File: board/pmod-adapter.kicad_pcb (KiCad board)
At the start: 2 copper layers, 20.3 x 86.4 mm, 28 parts

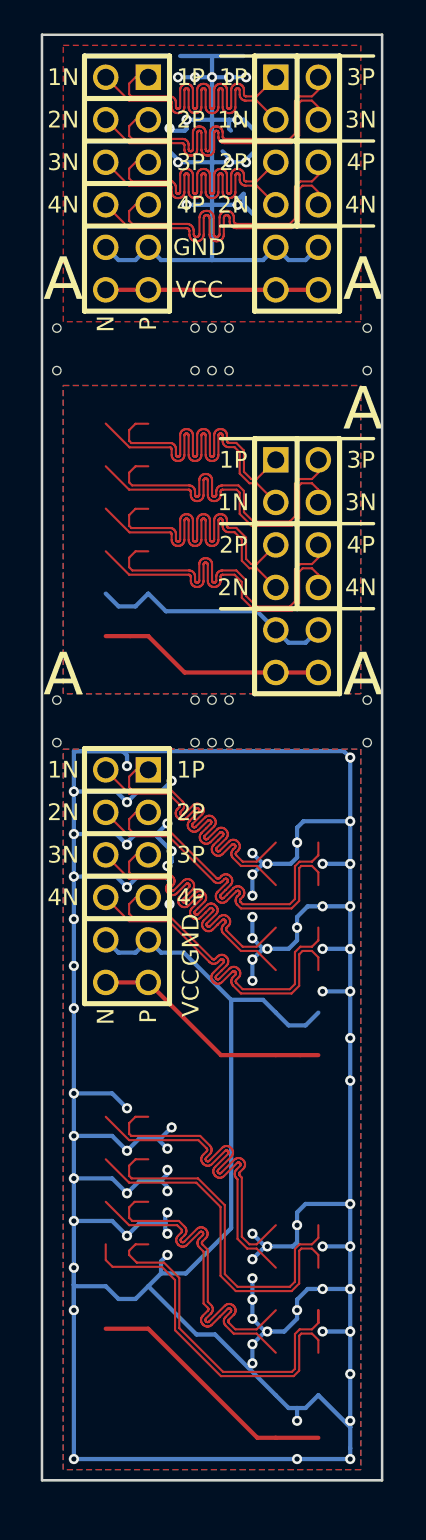
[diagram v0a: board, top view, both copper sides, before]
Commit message: Adding more gnd vias
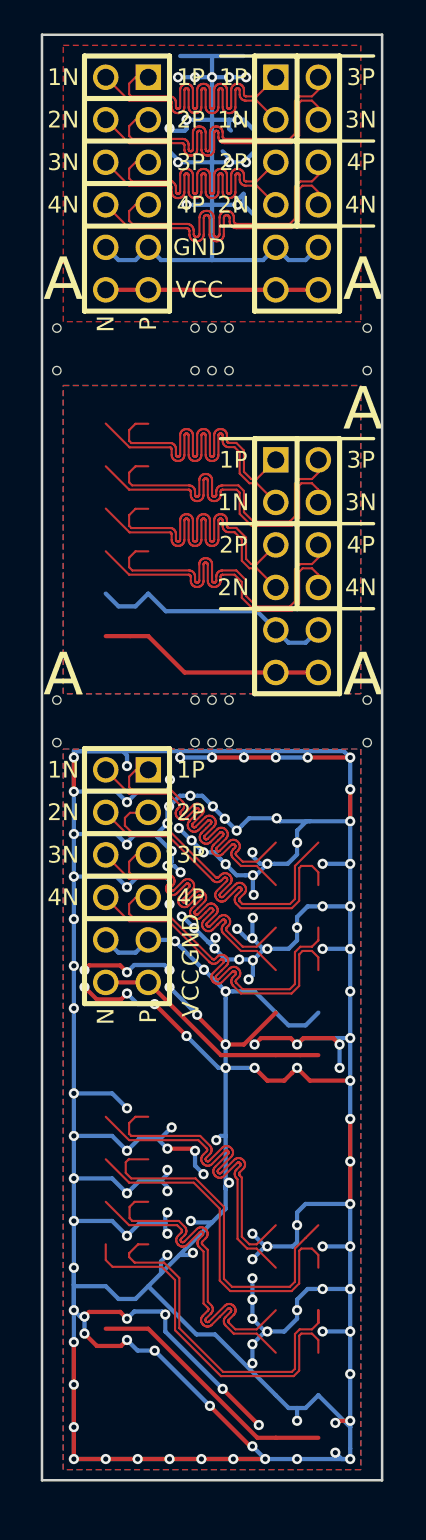
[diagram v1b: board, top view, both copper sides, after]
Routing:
- net /GND34: track 273.8 -> 429.2 mm, vias 73 -> 151
- net (no net): track 10.4 -> 0.00 mm, vias 6 -> 0

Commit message: Temp commit.
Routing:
- net /GND34: track 429.2 -> 452.3 mm, vias 151 -> 166
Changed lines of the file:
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@@
     (thickness 1.6)
     (drawings 28)
-    (tracks 3609)
+    (tracks 3656)
     (zones 0)
     (modules 32)
@@
   (segment (start 48.386999 76.326999) (end 49.53 77.47) (width 0.127) (layer F.Cu) (net 26))
   (segment (start 39.37 70.612) (end 40.767 72.009) (width 0.127) (layer F.Cu) (net 26))
+  (segment (start 37.5666 92.5576) (end 39.37 92.5576) (width 0.254) (layer B.Cu) (net 27))
+  (segment (start 39.37 92.5576) (end 39.8526 92.5576) (width 0.254) (layer B.Cu) (net 27))
+  (via (at 39.37 92.5576) (size 0.6096) (drill 0.3048) (layers F.Cu B.Cu) (net 27))
+  (segment (start 37.5412 89.9922) (end 39.37 89.9922) (width 0.254) (layer B.Cu) (net 27))
+  (segment (start 39.37 89.9922) (end 39.8272 89.9922) (width 0.254) (layer B.Cu) (net 27))
+  (via (at 39.37 89.9922) (size 0.6096) (drill 0.3048) (layers F.Cu B.Cu) (net 27))
+  (segment (start 37.5666 87.4776) (end 39.37 87.4776) (width 0.254) (layer B.Cu) (net 27))
+  (segment (start 39.37 87.4776) (end 39.8526 87.4776) (width 0.254) (layer B.Cu) (net 27))
+  (via (at 39.37 87.4776) (size 0.6096) (drill 0.3048) (layers F.Cu B.Cu) (net 27))
+  (segment (start 37.465 84.836) (end 37.5666 84.9376) (width 0.254) (layer B.Cu) (net 27))
+  (segment (start 37.5666 84.9376) (end 39.8526 84.9376) (width 0.254) (layer B.Cu) (net 27))
+  (segment (start 39.8526 84.9376) (end 40.64 85.725) (width 0.254) (layer B.Cu) (net 27))
+  (segment (start 37.465 92.456) (end 37.5666 92.5576) (width 0.254) (layer B.Cu) (net 27))
+  (segment (start 39.8526 92.5576) (end 40.64 93.345) (width 0.254) (layer B.Cu) (net 27))
+  (segment (start 37.465 89.916) (end 37.5412 89.9922) (width 0.254) (layer B.Cu) (net 27))
+  (segment (start 39.8272 89.9922) (end 40.64 90.805) (width 0.254) (layer B.Cu) (net 27))
+  (segment (start 37.465 87.376) (end 37.5666 87.4776) (width 0.254) (layer B.Cu) (net 27))
+  (segment (start 39.8526 87.4776) (end 40.64 88.265) (width 0.254) (layer B.Cu) (net 27))
+  (segment (start 52.07 102.87) (end 51.1556 101.9556) (width 0.254) (layer F.Cu) (net 27))
+  (via (at 51.1556 101.9556) (size 0.6096) (drill 0.3048) (layers F.Cu B.Cu) (net 27))
+  (segment (start 46.355 102.489) (end 47.8536 102.489) (width 0.254) (layer F.Cu) (net 27))
+  (segment (start 47.8536 102.489) (end 48.0314 102.3112) (width 0.254) (layer F.Cu) (net 27))
+  (via (at 48.0314 102.3112) (size 0.6096) (drill 0.3048) (layers F.Cu B.Cu) (net 27))
+  (segment (start 44.577 94.361) (end 44.577 95.1992) (width 0.254) (layer F.Cu) (net 27))
+  (segment (start 44.577 95.1992) (end 44.2468 95.5294) (width 0.254) (layer F.Cu) (net 27))
+  (via (at 44.2468 95.5294) (size 0.6096) (drill 0.3048) (layers F.Cu B.Cu) (net 27))
+  (segment (start 46.6344 100.8888) (end 44.3484 98.6028) (width 0.254) (layer B.Cu) (net 27))
+  (via (at 44.3484 98.6028) (size 0.6096) (drill 0.3048) (layers F.Cu B.Cu) (net 27))
+  (segment (start 48.133 100.965) (end 46.7106 100.965) (width 0.254) (layer F.Cu) (net 27))
+  (segment (start 46.7106 100.965) (end 46.6344 100.8888) (width 0.254) (layer F.Cu) (net 27))
+  (via (at 46.6344 100.8888) (size 0.6096) (drill 0.3048) (layers F.Cu B.Cu) (net 27))
+  (segment (start 53.975 78.74) (end 53.34 78.74) (width 0.254) (layer F.Cu) (net 27))
+  (segment (start 53.34 78.74) (end 52.07 80.01) (width 0.254) (layer F.Cu) (net 27))
+  (segment (start 43.8404 71.628) (end 44.577 71.628) (width 0.254) (layer B.Cu) (net 27))
+  (segment (start 44.577 71.628) (end 45.1612 72.2122) (width 0.254) (layer B.Cu) (net 27))
+  (via (at 45.1612 72.2122) (size 0.6096) (drill 0.3048) (layers F.Cu B.Cu) (net 27))
+  (segment (start 48.133 93.218) (end 48.133 89.7636) (width 0.254) (layer F.Cu) (net 27))
+  (segment (start 48.133 89.7636) (end 48.0314 89.662) (width 0.254) (layer F.Cu) (net 27))
+  (via (at 48.0314 89.662) (size 0.6096) (drill 0.3048) (layers F.Cu B.Cu) (net 27))
+  (segment (start 46.9392 95.6818) (end 46.9392 94.0562) (width 0.254) (layer B.Cu) (net 27))
+  (segment (start 46.9392 94.0562) (end 46.9646 94.0308) (width 0.254) (layer B.Cu) (net 27))
+  (via (at 46.9646 94.0308) (size 0.6096) (drill 0.3048) (layers F.Cu B.Cu) (net 27))
+  (segment (start 48.133 95.885) (end 47.1424 95.885) (width 0.254) (layer B.Cu) (net 27))
+  (segment (start 47.1424 95.885) (end 46.9392 95.6818) (width 0.254) (layer B.Cu) (net 27))
+  (via (at 46.9392 95.6818) (size 0.6096) (drill 0.3048) (layers F.Cu B.Cu) (net 27))
+  (segment (start 44.0817 98.5266) (end 41.91 96.3549) (width 0.254) (layer B.Cu) (net 27))
+  (segment (start 44.7929 99.2378) (end 44.0817 98.5266) (width 0.254) (layer B.Cu) (net 27))
+  (segment (start 44.0817 98.5266) (end 44.0817 98.4631) (width 0.254) (layer B.Cu) (net 27))
+  (segment (start 44.0817 98.4631) (end 44.8056 97.7392) (width 0.254) (layer B.Cu) (net 27))
+  (via (at 44.8056 97.7392) (size 0.6096) (drill 0.3048) (layers F.Cu B.Cu) (net 27))
+  (segment (start 45.8978 99.2378) (end 45.9232 99.2378) (width 0.254) (layer B.Cu) (net 27))
+  (via (at 46.101 99.06) (size 0.6096) (drill 0.3048) (layers F.Cu B.Cu) (net 27))
+  (segment (start 45.9232 99.2378) (end 46.101 99.06) (width 0.254) (layer B.Cu) (net 27))
+  (segment (start 48.133 97.155) (end 46.101 97.155) (width 0.254) (layer B.Cu) (net 27))
+  (segment (start 46.101 97.155) (end 46.0756 97.1296) (width 0.254) (layer B.Cu) (net 27))
+  (via (at 46.0756 97.1296) (size 0.6096) (drill 0.3048) (layers F.Cu B.Cu) (net 27))
   (via (at 45.212 89.662) (size 0.6096) (drill 0.3048) (layers F.Cu B.Cu) (net 27))
   (segment (start 44.704 88.265) (end 44.704 89.154) (width 0.254) (layer B.Cu) (net 27))
@@
   (segment (start 53.975 76.2) (end 52.324 76.2) (width 0.254) (layer B.Cu) (net 27))
   (via (at 52.324 76.2) (size 0.6096) (drill 0.3048) (layers F.Cu B.Cu) (net 27))
-  (segment (start 37.465 92.456) (end 39.751 92.456) (width 0.254) (layer B.Cu) (net 27))
-  (segment (start 39.751 92.456) (end 40.64 93.345) (width 0.254) (layer B.Cu) (net 27))
   (via (at 40.64 93.345) (size 0.6096) (drill 0.3048) (layers F.Cu B.Cu) (net 27))
-  (segment (start 37.465 84.836) (end 39.751 84.836) (width 0.254) (layer B.Cu) (net 27))
   (via (at 40.64 85.725) (size 0.6096) (drill 0.3048) (layers F.Cu B.Cu) (net 27))
-  (segment (start 39.751 84.836) (end 40.64 85.725) (width 0.254) (layer B.Cu) (net 27))
-  (segment (start 37.465 87.376) (end 39.751 87.376) (width 0.254) (layer B.Cu) (net 27))
-  (segment (start 39.751 87.376) (end 40.64 88.265) (width 0.254) (layer B.Cu) (net 27))
   (via (at 40.64 88.265) (size 0.6096) (drill 0.3048) (layers F.Cu B.Cu) (net 27))
-  (segment (start 37.465 89.916) (end 39.751 89.916) (width 0.254) (layer B.Cu) (net 27))
   (via (at 40.64 90.805) (size 0.6096) (drill 0.3048) (layers F.Cu B.Cu) (net 27))
-  (segment (start 39.751 89.916) (end 40.64 90.805) (width 0.254) (layer B.Cu) (net 27))
   (segment (start 51.308001 103.631999) (end 50.8 103.631999) (width 0.254) (layer B.Cu) (net 27))
   (segment (start 50.8 103.631999) (end 50.291999 103.631999) (width 0.254) (layer B.Cu) (net 27))
@@
   (segment (start 40.131999 97.116899) (end 39.37 96.3549) (width 0.254) (layer B.Cu) (net 27))
   (segment (start 45.8978 99.2378) (end 44.7929 99.2378) (width 0.254) (layer B.Cu) (net 27))
-  (segment (start 44.7929 99.2378) (end 41.91 96.3549) (width 0.254) (layer B.Cu) (net 27))
   (segment (start 49.53 102.87) (end 45.8978 99.2378) (width 0.254) (layer B.Cu) (net 27))
   (segment (start 52.07 102.87) (end 51.308001 103.631999) (width 0.254) (layer B.Cu) (net 27))

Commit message: Slowly adding more vias.
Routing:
- net /GND34: track 452.3 -> 457.4 mm, vias 166 -> 169
- net /J4D_N: track 21.5 -> 20.9 mm
- added copper zone on B.Cu, net /GND1
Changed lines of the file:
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@@
     (thickness 1.6)
     (drawings 28)
-    (tracks 3656)
+    (tracks 3666)
     (zones 0)
     (modules 32)
@@
   (segment (start 48.386999 76.326999) (end 49.53 77.47) (width 0.127) (layer F.Cu) (net 26))
   (segment (start 39.37 70.612) (end 40.767 72.009) (width 0.127) (layer F.Cu) (net 26))
+  (segment (start 48.5648 88.4428) (end 48.2346 88.1126) (width 0.254) (layer F.Cu) (net 27))
+  (segment (start 48.2346 88.1126) (end 47.5488 88.1126) (width 0.254) (layer F.Cu) (net 27))
+  (via (at 47.5488 88.1126) (size 0.6096) (drill 0.3048) (layers F.Cu B.Cu) (net 27))
+  (segment (start 48.5648 89.1286) (end 48.5648 88.4428) (width 0.254) (layer F.Cu) (net 27))
+  (segment (start 48.0314 89.662) (end 48.5648 89.1286) (width 0.254) (layer F.Cu) (net 27))
+  (segment (start 37.465 95.25) (end 38.2778 95.25) (width 0.254) (layer F.Cu) (net 27))
+  (segment (start 38.2778 95.25) (end 38.6334 94.8944) (width 0.254) (layer F.Cu) (net 27))
+  (via (at 38.6334 94.8944) (size 0.6096) (drill 0.3048) (layers F.Cu B.Cu) (net 27))
+  (segment (start 39.37 96.3549) (end 39.4081 96.3549) (width 0.254) (layer B.Cu) (net 27))
+  (segment (start 39.4081 96.3549) (end 40.2844 95.4786) (width 0.254) (layer B.Cu) (net 27))
+  (via (at 40.2844 95.4786) (size 0.6096) (drill 0.3048) (layers F.Cu B.Cu) (net 27))
   (segment (start 37.5666 92.5576) (end 39.37 92.5576) (width 0.254) (layer B.Cu) (net 27))
   (segment (start 39.37 92.5576) (end 39.8526 92.5576) (width 0.254) (layer B.Cu) (net 27))
@@
   (segment (start 52.07 99.568) (end 51.689 99.187) (width 0.127) (layer F.Cu) (net 34))
   (segment (start 51.689 99.187) (end 51.054 99.187) (width 0.127) (layer F.Cu) (net 34))
-  (segment (start 46.2534 101.727) (end 43.5102 98.9838) (width 0.127) (layer F.Cu) (net 34))
   (segment (start 51.054 99.187) (end 50.927 99.314) (width 0.127) (layer F.Cu) (net 34))
-  (segment (start 50.598604 101.727) (end 46.2534 101.727) (width 0.127) (layer F.Cu) (net 34))
   (segment (start 50.927 99.314) (end 50.927 101.398604) (width 0.127) (layer F.Cu) (net 34))
-  (segment (start 43.5102 98.9838) (end 43.5102 95.9866) (width 0.127) (layer F.Cu) (net 34))
-  (segment (start 50.927 101.398604) (end 50.598604 101.727) (width 0.127) (layer F.Cu) (net 34))
-  (segment (start 42.7228 95.1992) (end 39.7764 95.1992) (width 0.127) (layer F.Cu) (net 34))
   (segment (start 43.5102 95.9866) (end 42.7228 95.1992) (width 0.127) (layer F.Cu) (net 34))
-  (segment (start 39.7764 95.1992) (end 39.37 94.7928) (width 0.127) (layer F.Cu) (net 34))
-  (segment (start 39.37 94.7928) (end 39.37 93.853) (width 0.127) (layer F.Cu) (net 34))
+  (segment (start 50.927 101.398604) (end 50.598604 101.727) (width 0.127) (layer F.Cu) (net 34))
+  (segment (start 50.598604 101.727) (end 46.2534 101.727) (width 0.127) (layer F.Cu) (net 34))
+  (segment (start 43.5102 98.9838) (end 43.5102 95.9866) (width 0.127) (layer F.Cu) (net 34))
+  (segment (start 46.2534 101.727) (end 43.5102 98.9838) (width 0.127) (layer F.Cu) (net 34))
+  (segment (start 42.7228 95.1992) (end 40.7162 95.1992) (width 0.127) (layer F.Cu) (net 34))
+  (segment (start 40.7162 95.1992) (end 39.37 93.853) (width 0.127) (layer F.Cu) (net 34))
   (segment (start 43.58073 93.643416) (end 43.598617 93.721787) (width 0.127) (layer F.Cu) (net 35))
   (segment (start 43.635397 92.71) (end 43.889396 92.963999) (width 0.127) (layer F.Cu) (net 35))
@@
     (min_thickness 0.254)
     (keepout (tracks not_allowed) (vias not_allowed) (copperpour not_allowed))
-    (fill (arc_segments 16) (thermal_gap 0.508) (thermal_bridge_width 0.508))
+    (fill yes (arc_segments 16) (thermal_gap 0.508) (thermal_bridge_width 0.508))
     (polygon
       (pts
@@
     (min_thickness 0.254)
     (keepout (tracks not_allowed) (vias not_allowed) (copperpour not_allowed))
-    (fill (arc_segments 16) (thermal_gap 0.508) (thermal_bridge_width 0.508))
+    (fill yes (arc_segments 16) (thermal_gap 0.508) (thermal_bridge_width 0.508))
     (polygon
       (pts
@@
     (connect_pads (clearance 0.1905))
     (min_thickness 0.127)
-    (fill (arc_segments 16) (thermal_gap 0.508) (thermal_bridge_width 0.508))
+    (fill yes (arc_segments 16) (thermal_gap 0.508) (thermal_bridge_width 0.508))
     (polygon
       (pts
@@
     (connect_pads (clearance 0.1905))
     (min_thickness 0.127)
-    (fill (arc_segments 16) (thermal_gap 0.508) (thermal_bridge_width 0.508))
+    (fill yes (arc_segments 16) (thermal_gap 0.508) (thermal_bridge_width 0.508))
     (polygon
       (pts
@@
     (connect_pads (clearance 0.1905))
     (min_thickness 0.127)
-    (fill (arc_segments 16) (thermal_gap 0.508) (thermal_bridge_width 0.508))
+    (fill yes (arc_segments 16) (thermal_gap 0.508) (thermal_bridge_width 0.508))
     (polygon
       (pts
@@
     (connect_pads (clearance 0.1905))
     (min_thickness 0.127)
-    (fill (arc_segments 16) (thermal_gap 0.508) (thermal_bridge_width 0.508))
+    (fill yes (arc_segments 16) (thermal_gap 0.508) (thermal_bridge_width 0.508))
     (polygon
       (pts
@@
     (connect_pads (clearance 0.1905))
     (min_thickness 0.127)
-    (fill (arc_segments 16) (thermal_gap 0.508) (thermal_bridge_width 0.508))
+    (fill yes (arc_segments 16) (thermal_gap 0.508) (thermal_bridge_width 0.508))
     (polygon
       (pts
@@
       )
     )
+  )
+  (zone (net 1) (net_name /GND1) (layer B.Cu) (hatch edge 0.508)
+    (connect_pads (clearance 0.1905))
+    (min_thickness 0.127)
+    (fill yes (arc_segments 16) (thermal_gap 0.508) (thermal_bridge_width 0.508))
+    (polygon
+      (pts
+        (xy 54.61 38.735) (xy 36.83 38.735) (xy 36.83 22.225) (xy 54.61 22.225)
+      )
+    )

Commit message: Fixes.
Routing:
- net /GND2: track 14.9 -> 171.2 mm, vias 0 -> 80
- net /GND1: track 53.4 -> 176.6 mm, vias 13 -> 68
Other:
- board text added: "N2D"
- board text added: "v0.0"

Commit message: One more via.
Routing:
- net /GND1: track 176.6 -> 178.7 mm, vias 68 -> 69
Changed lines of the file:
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@@
     (thickness 1.6)
     (drawings 40)
-    (tracks 4016)
+    (tracks 4020)
     (zones 0)
     (modules 32)
@@
     (arrow2b (pts (xy 63.5 38.1) (xy 64.086421 39.226504)))
   )
+  (segment (start 46.99 34.1122) (end 46.7868 34.3154) (width 0.254) (layer F.Cu) (net 1))
+  (via (at 45.3898 34.3154) (size 0.6096) (drill 0.3048) (layers F.Cu B.Cu) (net 1))
+  (segment (start 46.7868 34.3154) (end 45.3898 34.3154) (width 0.254) (layer F.Cu) (net 1))
+  (segment (start 46.99 33.655) (end 46.99 34.1122) (width 0.254) (layer F.Cu) (net 1))
   (segment (start 50.8 38.1) (end 53.34 38.1) (width 0.254) (layer F.Cu) (net 1))
   (via (at 53.34 38.1) (size 0.6096) (drill 0.3048) (layers F.Cu B.Cu) (net 1))
